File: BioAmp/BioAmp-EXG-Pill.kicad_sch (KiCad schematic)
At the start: 42 parts, among them IC3 MAX1169BEUD+, J2 Conn_01x04_Pin, J3 Conn_01x04_Pin, J4 522710469, U1 TL074HIPWR

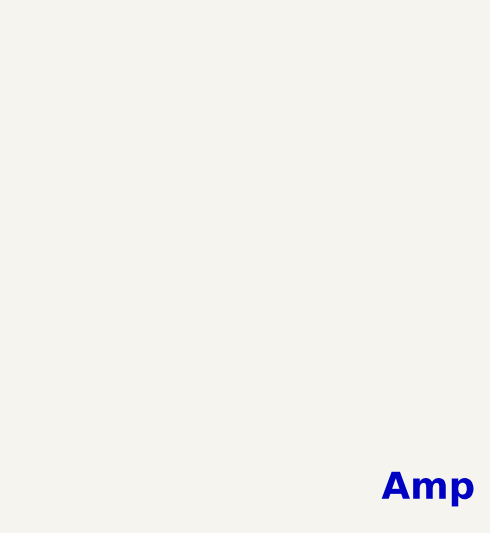
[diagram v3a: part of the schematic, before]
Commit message: Added rounded edge with mounting hole
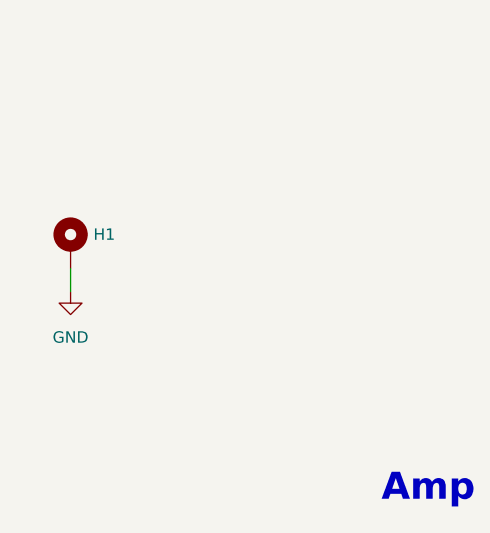
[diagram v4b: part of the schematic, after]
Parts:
- added H1: MountingHole_Pad, MountingHole:MountingHole_2mm, symbol Mechanical:MountingHole_Pad
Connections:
- net GND: now also H1.1
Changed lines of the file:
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@@
 	(wire
 		(pts
+			(xy 17.78 170.18) (xy 17.78 172.72)
+		)
+		(stroke
+			(width 0)
+			(type default)
+		)
+	)
+	(wire
+		(pts
 			(xy 107.95 29.21) (xy 113.03 29.21)
 		)
@@
 	)
 	(symbol
+		(lib_name "GND_3")
+		(lib_id "power:GND")
+		(at 17.78 172.72 0)
+		(unit 1)
+		(body_style 1)
+		(exclude_from_sim no)
+		(in_bom yes)
+		(on_board yes)
+		(in_pos_files yes)
+		(dnp no)
+		(fields_autoplaced yes)
+		(property "Reference" "#PWR03"
+			(at 17.78 179.07 0)
+			(hide yes)
+			(show_name no)
+			(do_not_autoplace no)
+			(effects
+				(font
+					(size 1.27 1.27)
+				)
+			)
+		)
+		(property "Value" "GND"
+			(at 17.78 177.8 0)
+			(show_name no)
+			(do_not_autoplace no)
+			(effects
+				(font
+					(size 1.27 1.27)
+				)
+			)
+		)
+		(property "Footprint" ""
+			(at 17.78 172.72 0)
+			(hide yes)
+			(show_name no)
+			(do_not_autoplace no)
+			(effects
+				(font
+					(size 1.27 1.27)
+				)
+			)
+		)
+		(property "Datasheet" ""
+			(at 17.78 172.72 0)
+			(hide yes)
+			(show_name no)
+			(do_not_autoplace no)
+			(effects
+				(font
+					(size 1.27 1.27)
+				)
+			)
+		)
+		(property "Description" "Power symbol creates a global label with name \"GND\" , ground"
+			(at 17.78 172.72 0)
+			(hide yes)
+			(show_name no)
+			(do_not_autoplace no)
+			(effects
+				(font
+					(size 1.27 1.27)
+				)
+			)
+		)
+		(pin "1"
+		)
+		(instances
+			(project "BioAmp-EXG-Pill"
+				(path "/6820f13c-3971-4615-b87b-c2f927031906"
+					(reference "#PWR03")
+					(unit 1)
+				)
+			)
+		)
+	)
+	(symbol
 		(lib_name "GND_7")
 		(lib_id "power:GND")
@@
 					(unit 1)
 				)
+			)
+		)
+	)
+	(symbol
+		(lib_id "Mechanical:MountingHole_Pad")
+		(at 17.78 167.64 0)
+		(unit 1)
+		(body_style 1)
+		(exclude_from_sim no)
+		(in_bom no)
+		(on_board yes)
+		(in_pos_files yes)
+		(dnp no)
+		(fields_autoplaced yes)
+		(property "Reference" "H1"
+			(at 20.32 166.3699 0)
+			(show_name no)
+			(do_not_autoplace no)
+			(effects
+				(font
+					(size 1.27 1.27)
+				)
+				(justify left)
+			)
+		)
+		(property "Value" "MountingHole_Pad"
+			(at 20.32 167.6399 0)
+			(hide yes)
+			(show_name no)
+			(do_not_autoplace no)
+			(effects
+				(font
+					(size 1.27 1.27)
+				)
+				(justify left)
+			)
+		)
+		(property "Footprint" "MountingHole:MountingHole_2mm"
+			(at 17.78 167.64 0)
+			(hide yes)
+			(show_name no)
+			(do_not_autoplace no)
+			(effects
+				(font
+					(size 1.27 1.27)
+				)
+			)
+		)
+		(property "Datasheet" ""
+			(at 17.78 167.64 0)
+			(hide yes)
+			(show_name no)
+			(do_not_autoplace no)
+			(effects
+				(font
+					(size 1.27 1.27)
+				)
+			)
+		)
+		(property "Description" "Mounting Hole with connection"
+			(at 17.78 167.64 0)
+			(hide yes)
+			(show_name no)
+			(do_not_autoplace no)
+			(effects
+				(font
+					(size 1.27 1.27)
+				)
+			)
+		)
+		(pin "1"
+		)
+		(instances
+			(project "BioAmp-EXG-Pill"
+				(path "/6820f13c-3971-4615-b87b-c2f927031906"
+					(reference "H1")
+					(unit 1)
+				)

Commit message: Changed I2C connectors, added mounting holes and roundes edge
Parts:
- C1: footprint Capacitor_SMD:C_0805_2012Metric_Pad1.18x1.45mm_HandSolder -> Capacitor_SMD:C_0603_1608Metric_Pad1.08x0.95mm_HandSolder
- J2, J3: footprint Connector_JST:JST_PH_B4B-PH-K_1x04_P2.00mm_Vertical -> I2C_Connector:CONN_5037630000-SD_04_MOL
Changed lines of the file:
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@@
 			)
 		)
-		(property "Footprint" "Capacitor_SMD:C_0805_2012Metric_Pad1.18x1.45mm_HandSolder"
+		(property "Footprint" "Capacitor_SMD:C_0603_1608Metric_Pad1.08x0.95mm_HandSolder"
 			(at 66.04 106.3752 0)
 			(hide yes)
@@
 			)
 		)
-		(property "Footprint" "Connector_JST:JST_PH_B4B-PH-K_1x04_P2.00mm_Vertical"
+		(property "Footprint" "I2C_Connector:CONN_5037630000-SD_04_MOL"
 			(at 190.5 87.63 0)
 			(hide yes)
@@
 			)
 		)
-		(property "Footprint" "Connector_JST:JST_PH_B4B-PH-K_1x04_P2.00mm_Vertical"
+		(property "Footprint" "I2C_Connector:CONN_5037630000-SD_04_MOL"
 			(at 262.89 87.63 0)
 			(hide yes)

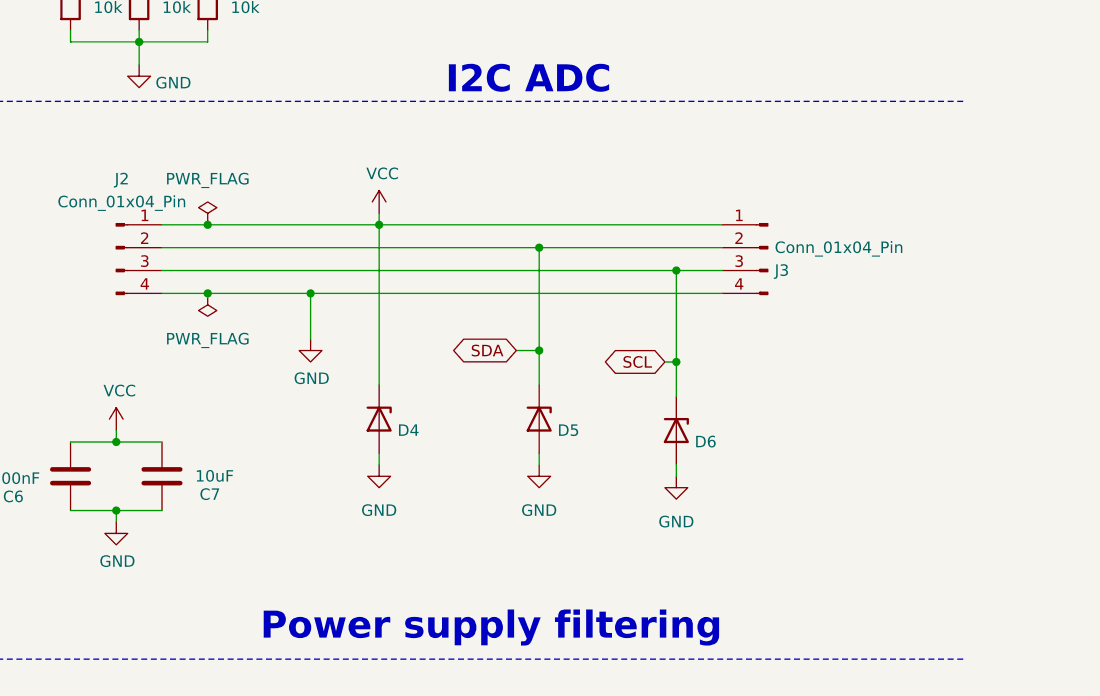
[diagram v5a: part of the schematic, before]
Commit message: Save BioAmp layout before splitting analog and digital grounds
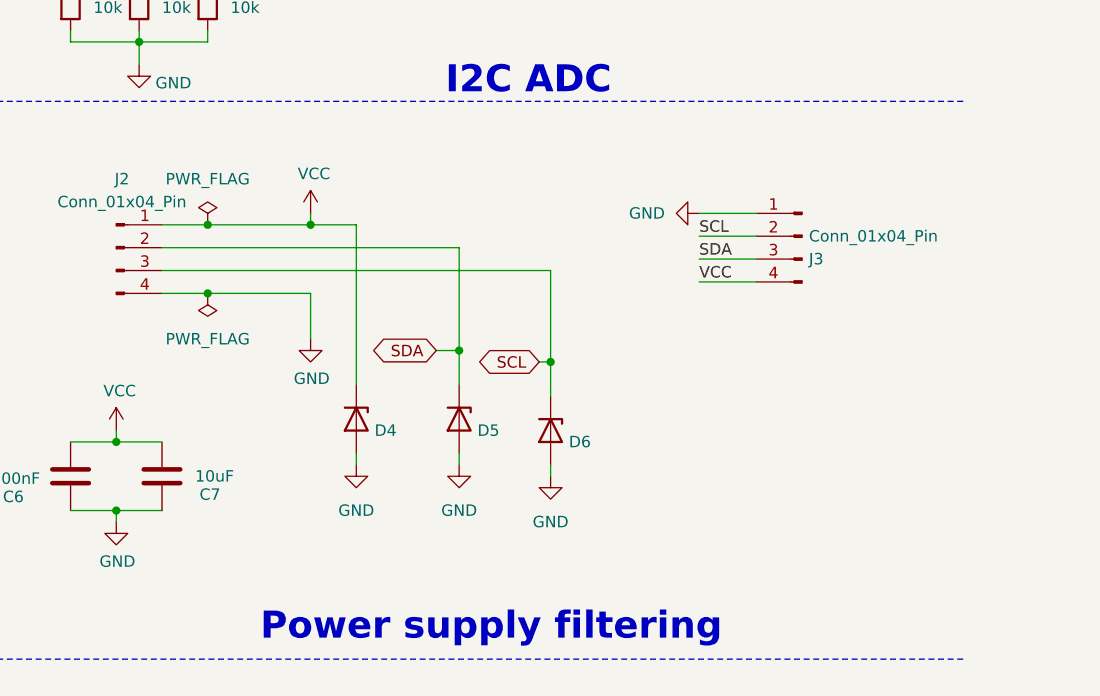
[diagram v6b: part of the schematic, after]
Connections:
- net GND: now also J3.1 (Pin_1); no longer J3.4 (Pin_4)
- net SCL: now also J3.2 (Pin_2); no longer J3.3 (Pin_3)
- net SDA: now also J3.3 (Pin_3); no longer J3.2 (Pin_2)
- net VCC: now also J3.4 (Pin_4); no longer J3.1 (Pin_1)
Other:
- moved on the sheet: D4, D5, D6, J3

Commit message: Separated analog and digital grounds in schematic
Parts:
- added NT1: NetTie_2, NetTie:NetTie-2_SMD_Pad0.5mm, symbol Device:NetTie_2
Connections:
- net GND: now also NT1.1; no longer C11.1, C12.1, C3.2, C6.1, C7.1, C9.1, D1.2 (A), D2.2 (A), D3.2 (A), IC3.11 (AGNDS), IC3.9 (AGND), R9.1, U1.11 (V-)
- new net GNDA: C11.1, C12.1, C3.2, C6.1, C7.1, C9.1, D1.2 (A), D2.2 (A), D3.2 (A), IC3.11 (AGNDS), IC3.9 (AGND), NT1.2, R9.1, U1.11 (V-)

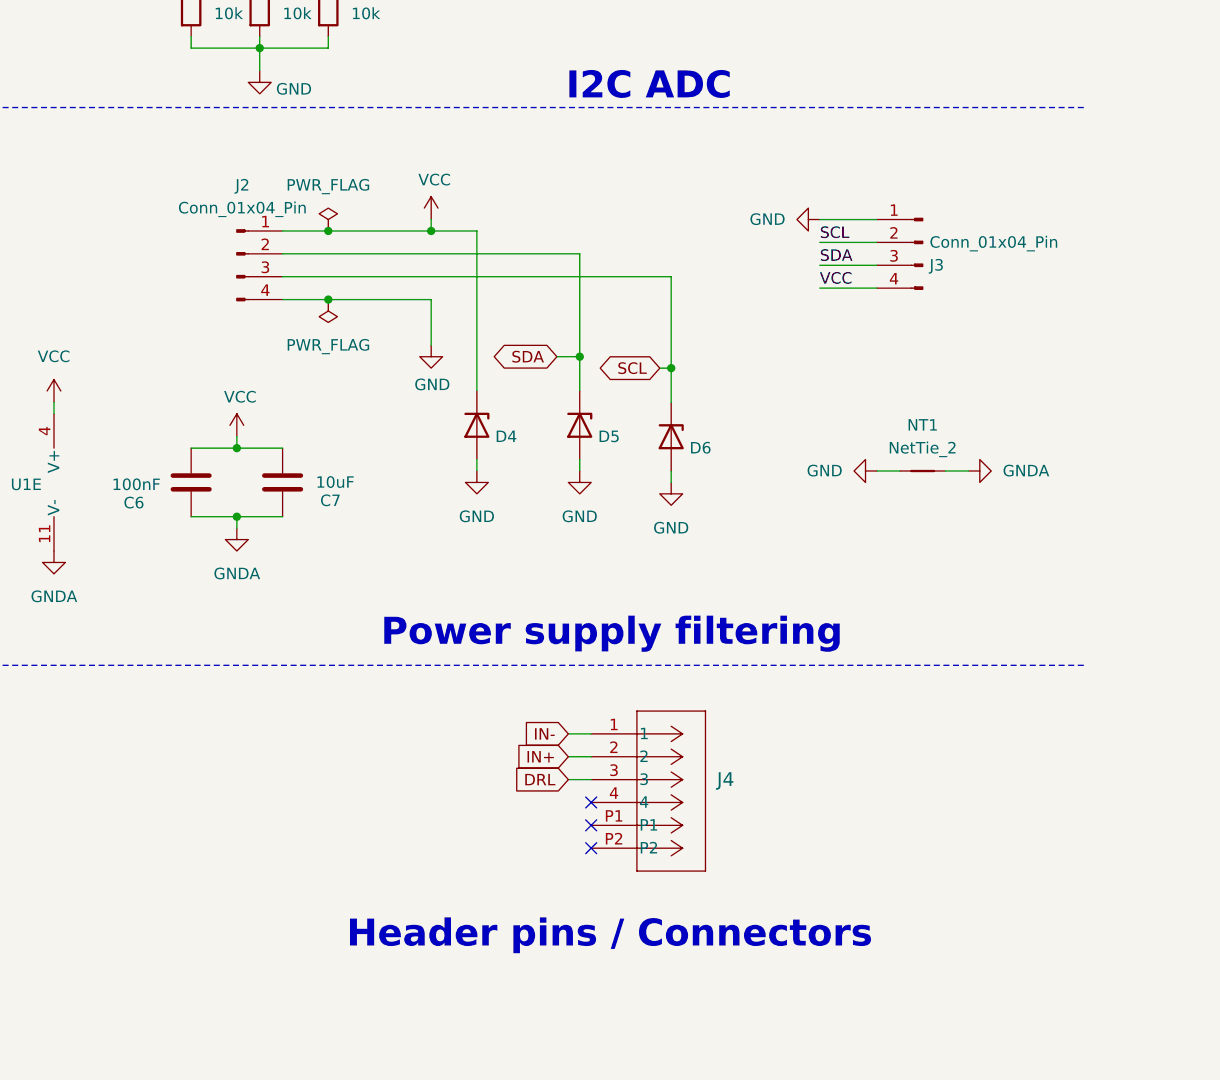
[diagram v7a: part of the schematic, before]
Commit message: Finished first layout with separated analog and digital grounds
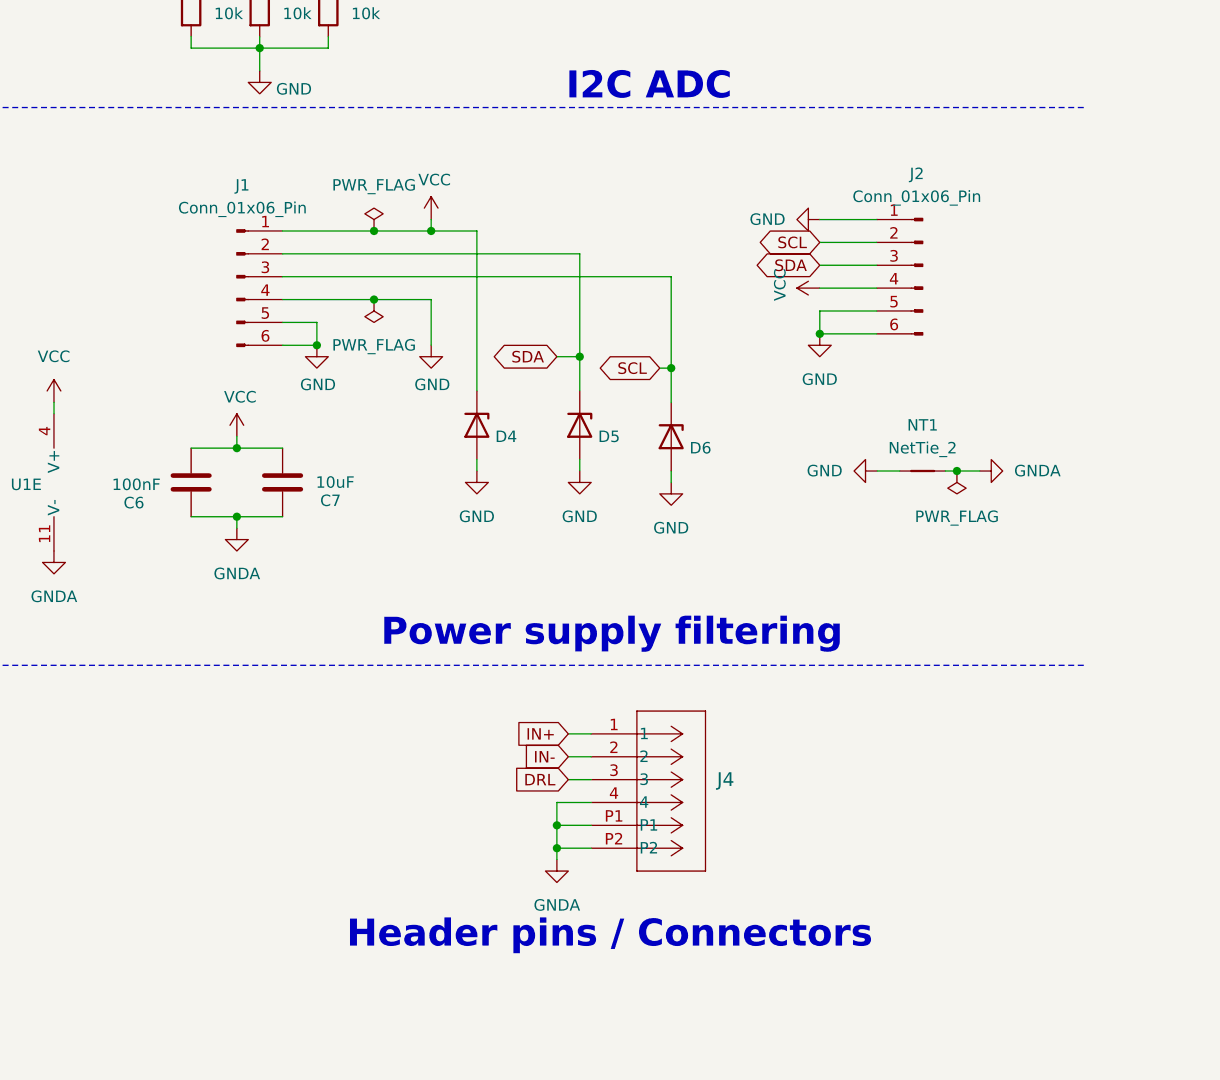
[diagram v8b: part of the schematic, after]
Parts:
- removed J2, J3: Conn_01x04_Pin, I2C_Connector:CONN_5037630000-SD_04_MOL, symbol Connector:Conn_01x04_Pin
- added J1, J2: Conn_01x06_Pin, I2C_Connector:CONN_5037630000-SD_04_MOL, symbol Connector:Conn_01x06_Pin
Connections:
- net GND: now also J1.4 (Pin_4), J1.5 (Pin_5), J1.6 (Pin_6), J2.1 (Pin_1), J2.5 (Pin_5), J2.6 (Pin_6)
- net GNDA: now also J4.4, J4.P1, J4.P2
- net IN+: now also J4.1; no longer J4.2
- net IN-: now also J4.2; no longer J4.1
- net SCL: now also J1.3 (Pin_3), J2.2 (Pin_2)
- net SDA: now also J1.2 (Pin_2), J2.3 (Pin_3)
- net VCC: now also J1.1 (Pin_1), J2.4 (Pin_4)
- no-connect marks 3 -> 0
